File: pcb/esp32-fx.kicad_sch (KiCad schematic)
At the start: 97 parts, among them J1 AudioJack2 (out), J2 AudioJack2 (in), J3 Jack-DC, J4 Raspberry_Pi_4, J5 AudioJack2 (in), J6 AudioJack2 (out), K1 G6K-2, Q1 MMBT2222A, Q2 MMBT2222A, Q3 MMBT2222A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

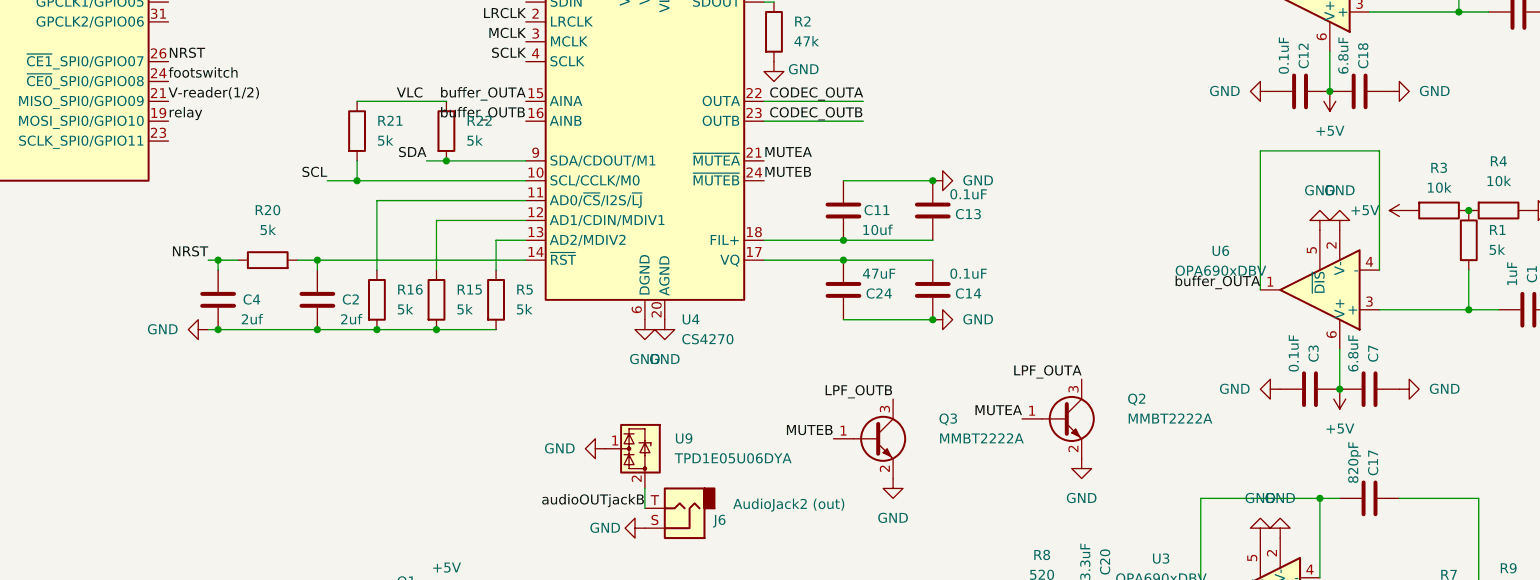
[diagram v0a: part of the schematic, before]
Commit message: wrote I2C I2S and using multible cores
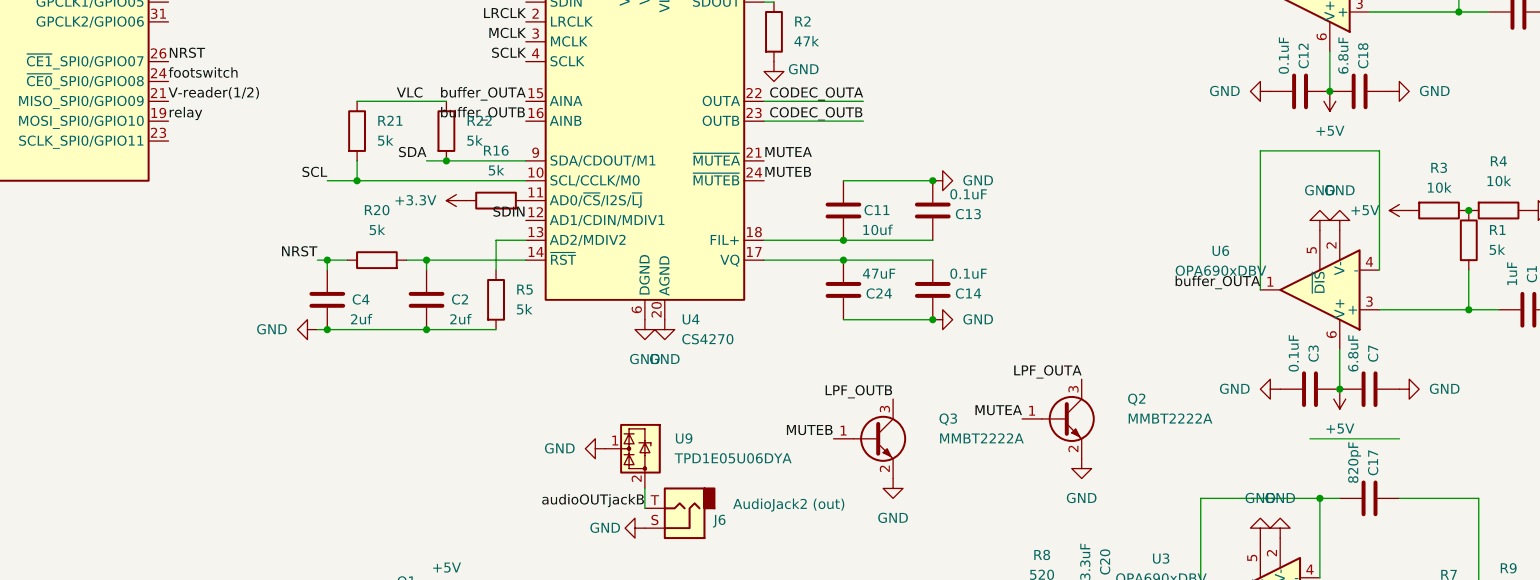
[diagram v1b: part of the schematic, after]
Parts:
- removed R15: 5k, Resistor_SMD:R_0603_1608Metric, symbol Device:R
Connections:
- net +3.3V: now also R16.1
- net GND: no longer R16.2
- net SDIN: now also U4.12 (AD1/CDIN/MDIV1)
- net at U4.11 (AD0/~{CS}/I2S/~{LJ}): now also R16.2; no longer R16.1
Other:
- moved on the sheet: C2, C4, R16, R20
